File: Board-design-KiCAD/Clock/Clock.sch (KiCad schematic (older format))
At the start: 48 parts, among them M1 SevSeg4Inch, M2 SevSeg4Inch, Y1 SevSeg1.8Inch, Y2 SevSeg1.8Inch, Y3 SevSeg1.8Inch, Y4 SevSeg1.8Inch

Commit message: Update part(s): DS3231 RTC Module
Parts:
- removed RTC1: DS3231-RPi, Custom:DS3231-RPi, symbol Custom:DS3231-RPi
- added RTC1: DS3231-Module, Custom:DS3231-Module, symbol Custom:DS3231-Module
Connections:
- wire segments 281 -> 282
- no-connect marks 51 -> 55
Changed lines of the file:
@@
 Text GLabel 3500 4300 2    50   Input ~ 0
 RTC_SDA
-Text GLabel 1800 8000 2    50   Input ~ 0
+Text GLabel 1800 7900 2    50   Input ~ 0
 RTC_SDA
 Text GLabel 2400 3850 0    50   Input ~ 0
 +3.3V
-Text GLabel 1200 7900 0    50   Input ~ 0
+Text GLabel 1200 7800 0    50   Input ~ 0
 +3.3V
 $Comp
 L power:GND #PWR03
 U 1 1 5F82DF5B
-P 1100 8400
-F 0 "#PWR03" H 1100 8150 50  0001 C CNN
-F 1 "GND" H 1105 8227 50  0000 C CNN
-F 2 "" H 1100 8400 50  0001 C CNN
-F 3 "" H 1100 8400 50  0001 C CNN
-	1    1100 8400
+P 1800 8600
+F 0 "#PWR03" H 1800 8350 50  0001 C CNN
+F 1 "GND" H 1805 8427 50  0000 C CNN
+F 2 "" H 1800 8600 50  0001 C CNN
+F 3 "" H 1800 8600 50  0001 C CNN
+	1    1800 8600
 	1    0    0    -1
 $EndComp
@@
 NoConn ~ 3400 6750
 NoConn ~ 3400 6850
-$Comp
-L Custom:DS3231-RPi RTC1
-U 1 1 5F952233
-P 1500 8100
-F 0 "RTC1" H 1500 8565 50  0000 C CNN
-F 1 "DS3231-RPi" H 1500 8474 50  0000 C CNN
-F 2 "Custom:DS3231-RPi" H 1500 8200 50  0001 C CNN
-F 3 "" H 1500 8200 50  0001 C CNN
-	1    1500 8100
-	1    0    0    -1
-$EndComp
-Wire Wire Line
-	1100 8400 1100 8300
-Wire Wire Line
-	1100 8300 1200 8300
 $Comp
 L Regulator_Linear:LM1117-3.3 Regulator-3.3V1
@@
 	1    0    0    -1
 $EndComp
+$Comp
+L Custom:DS3231-Module RTC1
+U 1 1 5F69BB73
+P 1500 8150
+F 0 "RTC1" H 1500 8765 50  0000 C CNN
+F 1 "DS3231-Module" H 1500 8674 50  0000 C CNN
+F 2 "Custom:DS3231-Module" H 1500 8400 50  0001 C CNN
+F 3 "" H 1500 8400 50  0001 C CNN
+	1    1500 8150
+	1    0    0    -1
+$EndComp
+Wire Wire Line
+	1800 8400 1800 8500
+Wire Wire Line
+	1800 8500 1800 8600
+Connection ~ 1800 8500
+Wire Wire Line
+	1200 7800 1200 7900
+NoConn ~ 1200 8350
+NoConn ~ 1200 8250
+NoConn ~ 1800 7800
+NoConn ~ 1800 8100
 Wire Bus Line
 	10450 2850 10450 3850

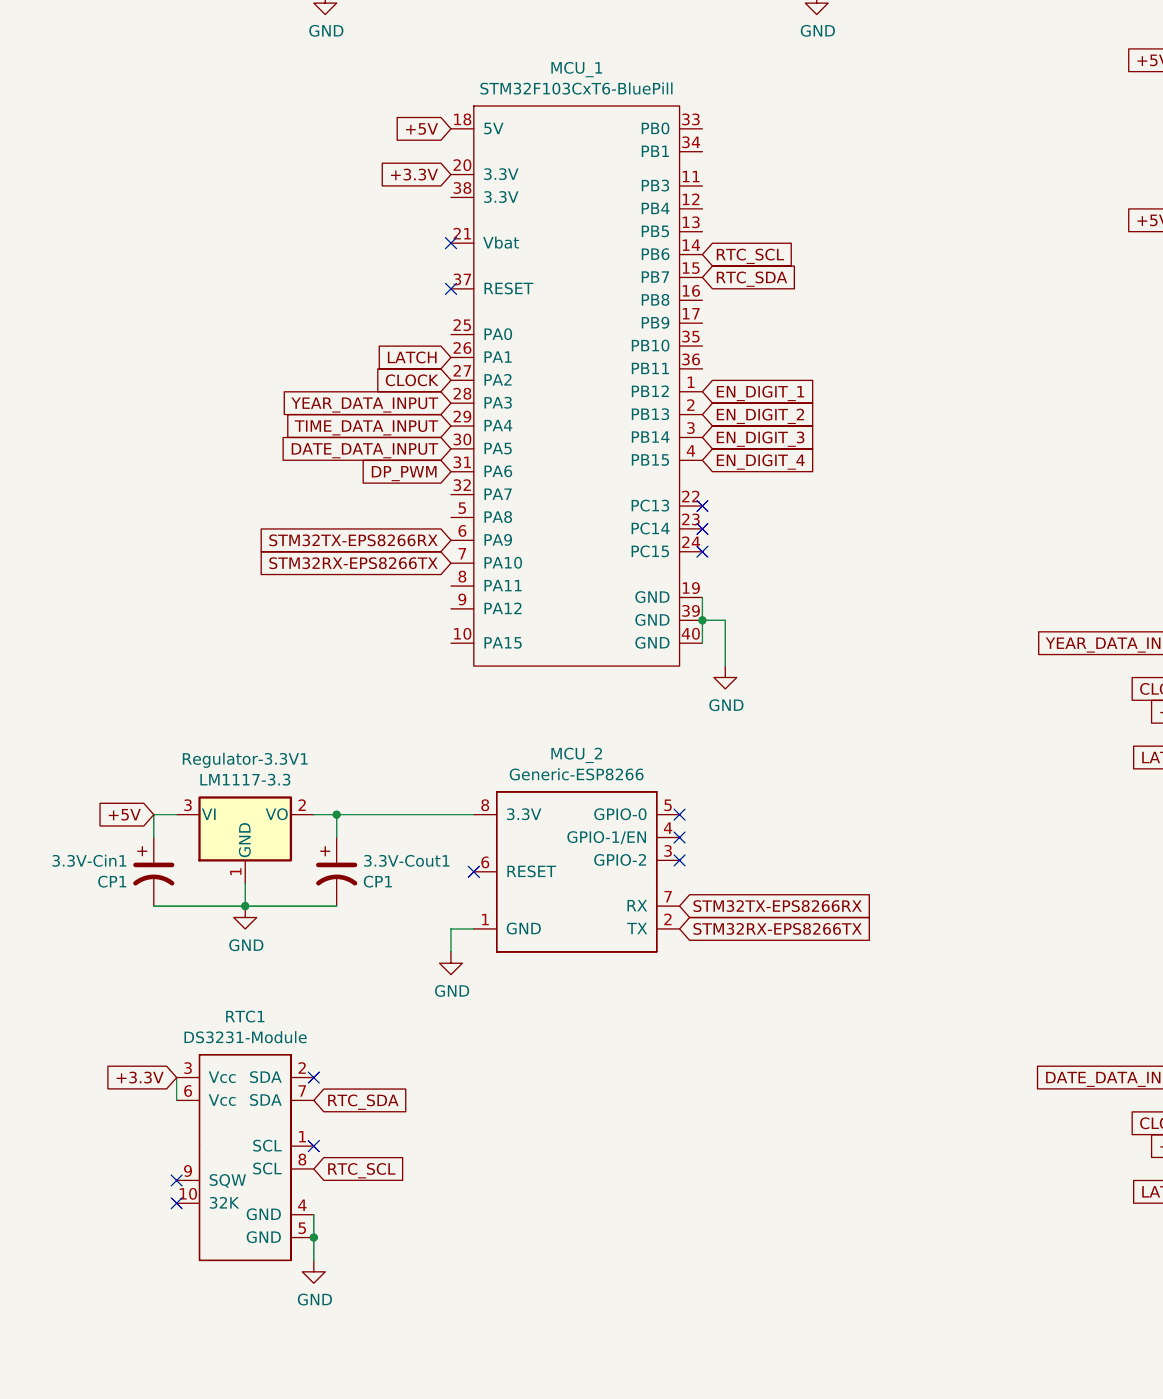
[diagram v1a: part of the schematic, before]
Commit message: Add credential reset button for ESP8266
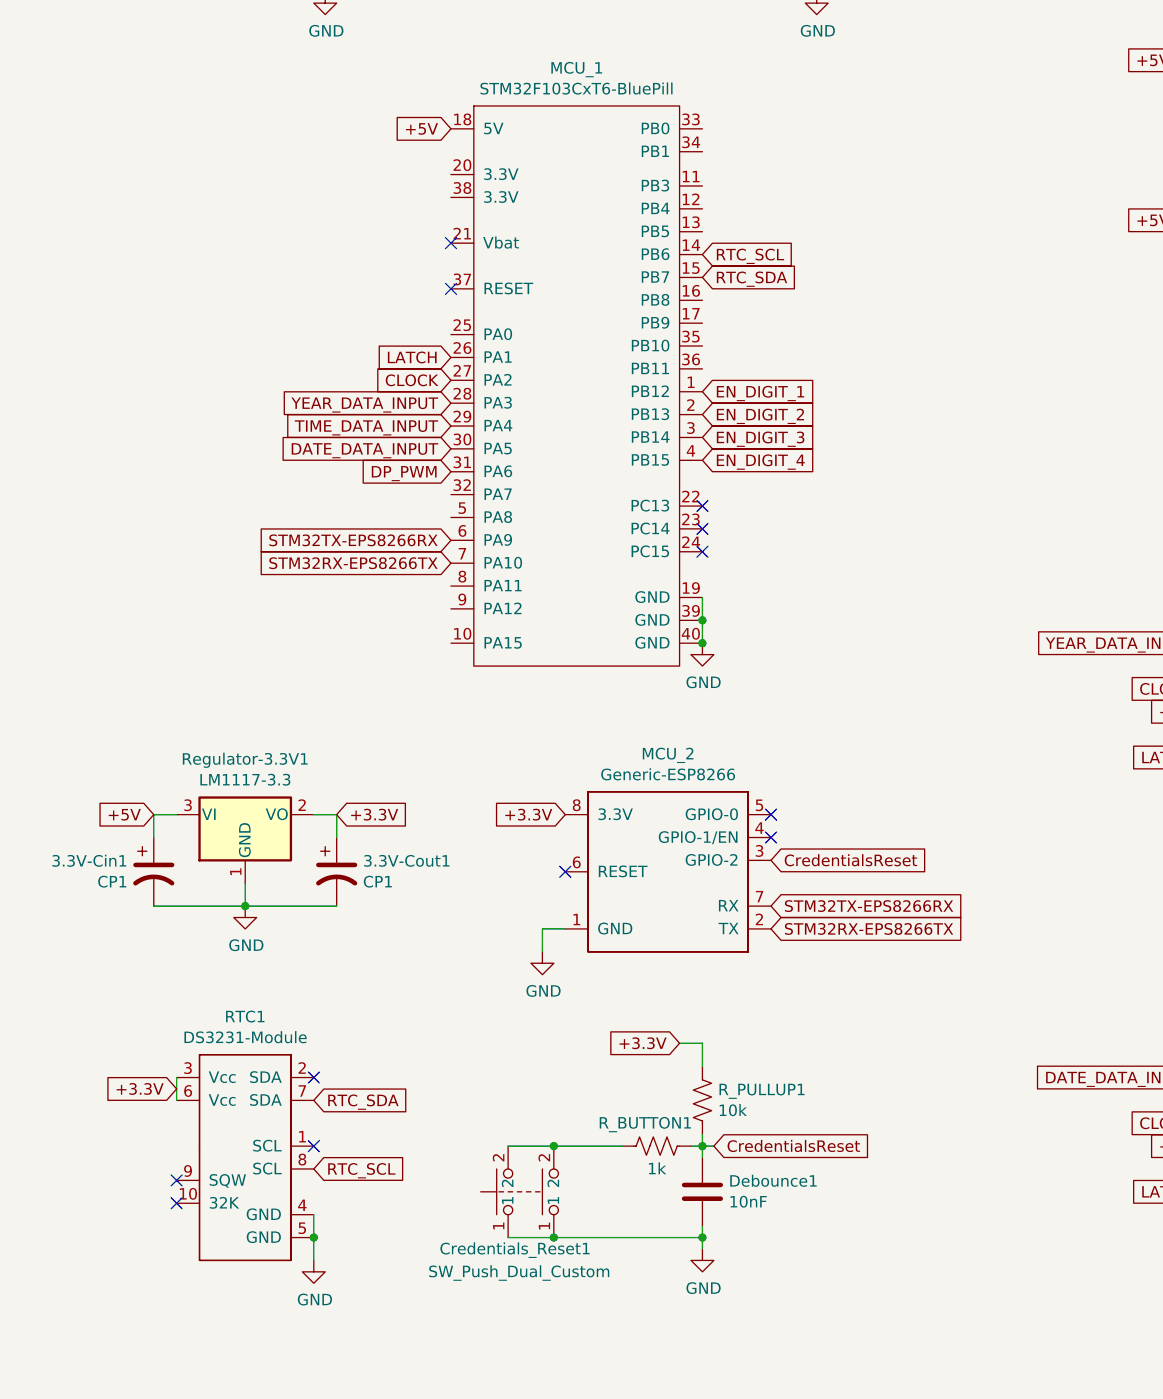
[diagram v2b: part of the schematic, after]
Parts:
- added Credentials_Reset1: SW_Push_Dual_Custom, Button_Switch_THT:SW_PUSH-12mm_Wuerth-430476085716, symbol Custom:SW_Push_Dual_Custom
- added Debounce1: 10nF, Capacitor_THT:C_Disc_D5.0mm_W2.5mm_P5.00mm, symbol Device:C
- added R_BUTTON1: 1k, Resistor_THT:R_Axial_DIN0207_L6.3mm_D2.5mm_P10.16mm_Horizontal, symbol Device:R_US
- added R_PULLUP1: 10k, Resistor_THT:R_Axial_DIN0207_L6.3mm_D2.5mm_P10.16mm_Horizontal, symbol Device:R_US
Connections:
- net +3.3V: now also 3.3V-Cout1.1, MCU_2.8 (3.3V), Regulator-3.3V1.2 (VO), R_PULLUP1.1; no longer MCU_1.20 (3.3V)
- net GND: now also Credentials_Reset1.1, Debounce1.2
- net CredentialsReset: now reaches MCU_2.3 (GPIO-2)
- net CredentialsReset: now also Debounce1.1, R_BUTTON1.2, R_PULLUP1.2
- new net: Credentials_Reset1.2, R_BUTTON1.1
- no-connect marks 55 -> 54
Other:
- moved on the sheet: MCU_2
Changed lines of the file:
@@
 L power:GND #PWR01
 U 1 1 5F6AF068
-P 3600 6000
-F 0 "#PWR01" H 3600 5750 50  0001 C CNN
-F 1 "GND" H 3605 5827 50  0000 C CNN
-F 2 "" H 3600 6000 50  0001 C CNN
-F 3 "" H 3600 6000 50  0001 C CNN
-	1    3600 6000
+P 3500 5900
+F 0 "#PWR01" H 3500 5650 50  0001 C CNN
+F 1 "GND" H 3505 5727 50  0000 C CNN
+F 2 "" H 3500 5900 50  0001 C CNN
+F 3 "" H 3500 5900 50  0001 C CNN
+	1    3500 5900
 	1    0    0    -1
 $EndComp
@@
 	3500 5800 3500 5900
 Connection ~ 3500 5800
-Wire Wire Line
-	3600 6000 3600 5800
-Wire Wire Line
-	3600 5800 3500 5800
 Text GLabel 2400 5150 0    50   Input ~ 0
 DP_PWM
@@
 L Custom:Generic-ESP8266 MCU_2
 U 1 1 5F825E1F
-P 2950 6750
-F 0 "MCU_2" H 2950 7115 50  0000 C CNN
-F 1 "Generic-ESP8266" H 2950 7024 50  0000 C CNN
-F 2 "Custom:Generic-ESP8266" H 2700 6750 50  0001 C CNN
-F 3 "" H 2700 6750 50  0001 C CNN
-	1    2950 6750
+P 3350 6750
+F 0 "MCU_2" H 3350 7115 50  0000 C CNN
+F 1 "Generic-ESP8266" H 3350 7024 50  0000 C CNN
+F 2 "Custom:Generic-ESP8266" H 3100 6750 50  0001 C CNN
+F 3 "" H 3100 6750 50  0001 C CNN
+	1    3350 6750
 	1    0    0    -1
 $EndComp
@@
 Text GLabel 1800 7900 2    50   Input ~ 0
 RTC_SDA
-Text GLabel 2400 3850 0    50   Input ~ 0
+Text GLabel 1900 6650 2    50   Input ~ 0
 +3.3V
-Text GLabel 1200 7800 0    50   Input ~ 0
+Text GLabel 1200 7850 0    50   Input ~ 0
 +3.3V
 $Comp
@@
 Text GLabel 2400 5550 0    50   Input ~ 0
 STM32RX-EPS8266TX
-Text GLabel 3400 7050 2    50   Input ~ 0
+Text GLabel 3800 7050 2    50   Input ~ 0
 STM32TX-EPS8266RX
-Text GLabel 3400 7150 2    50   Input ~ 0
+Text GLabel 3800 7150 2    50   Input ~ 0
 STM32RX-EPS8266TX
 $Comp
 L power:GND #PWR02
 U 1 1 5F84B160
-P 2400 7250
-F 0 "#PWR02" H 2400 7000 50  0001 C CNN
-F 1 "GND" H 2405 7077 50  0000 C CNN
-F 2 "" H 2400 7250 50  0001 C CNN
-F 3 "" H 2400 7250 50  0001 C CNN
-	1    2400 7250
-	1    0    0    -1
-$EndComp
-Wire Wire Line
-	2400 7250 2400 7150
-Wire Wire Line
-	2400 7150 2500 7150
-NoConn ~ 2500 6900
-NoConn ~ 3400 6650
-NoConn ~ 3400 6750
-NoConn ~ 3400 6850
+P 2800 7250
+F 0 "#PWR02" H 2800 7000 50  0001 C CNN
+F 1 "GND" H 2805 7077 50  0000 C CNN
+F 2 "" H 2800 7250 50  0001 C CNN
+F 3 "" H 2800 7250 50  0001 C CNN
+	1    2800 7250
+	1    0    0    -1
+$EndComp
+Wire Wire Line
+	2800 7250 2800 7150
+Wire Wire Line
+	2800 7150 2900 7150
+NoConn ~ 2900 6900
+NoConn ~ 3800 6650
+NoConn ~ 3800 6750
 $Comp
 L Regulator_Linear:LM1117-3.3 Regulator-3.3V1
@@
 Text GLabel 1100 6650 0    50   Input ~ 0
 +5V
-Wire Wire Line
-	1900 6650 2500 6650
-Connection ~ 1900 6650
 $Comp
 L power:GND #PWR04
@@
 NoConn ~ 1800 7800
 NoConn ~ 1800 8100
+Text GLabel 2900 6650 0    50   Input ~ 0
++3.3V
+$Comp
+L Device:C Debounce1
+U 1 1 5F763DEB
+P 3500 8300
+F 0 "Debounce1" H 3615 8346 50  0000 L CNN
+F 1 "10nF" H 3615 8255 50  0000 L CNN
+F 2 "Capacitor_THT:C_Disc_D5.0mm_W2.5mm_P5.00mm" H 3538 8150 50  0001 C CNN
+F 3 "~" H 3500 8300 50  0001 C CNN
+	1    3500 8300
+	1    0    0    -1
+$EndComp
+$Comp
+L power:GND #PWR0119
+U 1 1 5F765C62
+P 3500 8550
+F 0 "#PWR0119" H 3500 8300 50  0001 C CNN
+F 1 "GND" H 3505 8377 50  0000 C CNN
+F 2 "" H 3500 8550 50  0001 C CNN
+F 3 "" H 3500 8550 50  0001 C CNN
+	1    3500 8550
+	1    0    0    -1
+$EndComp
+$Comp
+L Device:R_US R_PULLUP1
+U 1 1 5F766377
+P 3500 7900
+F 0 "R_PULLUP1" H 3568 7946 50  0000 L CNN
+F 1 "10k" H 3568 7855 50  0000 L CNN
+F 2 "Resistor_THT:R_Axial_DIN0207_L6.3mm_D2.5mm_P10.16mm_Horizontal" V 3540 7890 50  0001 C CNN
+F 3 "~" H 3500 7900 50  0001 C CNN
+	1    3500 7900
+	1    0    0    -1
+$EndComp
+$Comp
+L Device:R_US R_BUTTON1
+U 1 1 5F767A96
+P 3300 8100
+F 0 "R_BUTTON1" V 3400 8150 50  0000 C CNN
+F 1 "1k" V 3200 8100 50  0000 C CNN
+F 2 "Resistor_THT:R_Axial_DIN0207_L6.3mm_D2.5mm_P10.16mm_Horizontal" V 3340 8090 50  0001 C CNN
+F 3 "~" H 3300 8100 50  0001 C CNN
+	1    3300 8100
+	0    -1   -1   0
+$EndComp
+Text GLabel 3400 7650 0    50   Input ~ 0
++3.3V
+Wire Wire Line
+	3500 8050 3500 8100
+Wire Wire Line
+	3500 8100 3450 8100
+Wire Wire Line
+	3500 8150 3500 8100
+Connection ~ 3500 8100
+Wire Wire Line
+	3400 7650 3500 7650
+Wire Wire Line
+	3500 7650 3500 7750
+Connection ~ 3500 5900
+Wire Wire Line
+	3500 8500 3500 8550
+Wire Wire Line
+	3500 8500 3500 8450
+Connection ~ 3500 8500
+Text GLabel 3550 8100 2    50   Input ~ 0
+CredentialsReset
+Text GLabel 3800 6850 2    50   Input ~ 0
+CredentialsReset
+Wire Wire Line
+	3550 8100 3500 8100
+Wire Wire Line
+	2850 8500 3500 8500
+Wire Wire Line
+	2850 8100 3150 8100
+$Comp
+L Custom:SW_Push_Dual_Custom Credentials_Reset1
+U 1 1 5F9F281E
+P 2700 8300
+F 0 "Credentials_Reset1" V 2450 8650 50  0000 R CNN
+F 1 "SW_Push_Dual_Custom" V 2350 8700 50  0000 R CNN
+F 2 "Button_Switch_THT:SW_PUSH-12mm_Wuerth-430476085716" H 2700 8300 50  0001 C CNN
+F 3 "" H 2700 8300 50  0001 C CNN
+	1    2700 8300
+	0    -1   -1   0
+$EndComp
+Wire Wire Line
+	2650 8500 2850 8500
+Connection ~ 2850 8500
+Wire Wire Line
+	2650 8100 2850 8100
 Wire Bus Line
 	10450 2850 10450 3850
@@
 Wire Bus Line
 	8800 7400 8800 8500
+Connection ~ 2850 8100
 $EndSCHEMATC

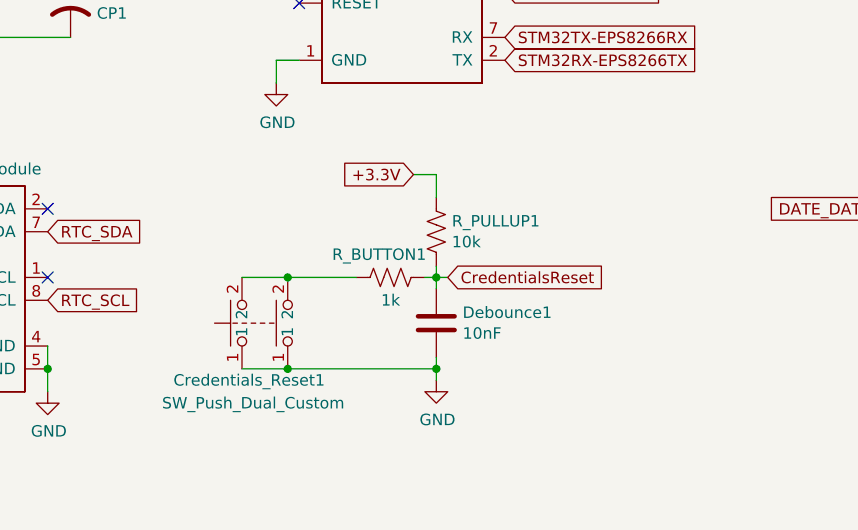
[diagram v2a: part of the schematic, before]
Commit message: Modify button circuit and build code for button management.
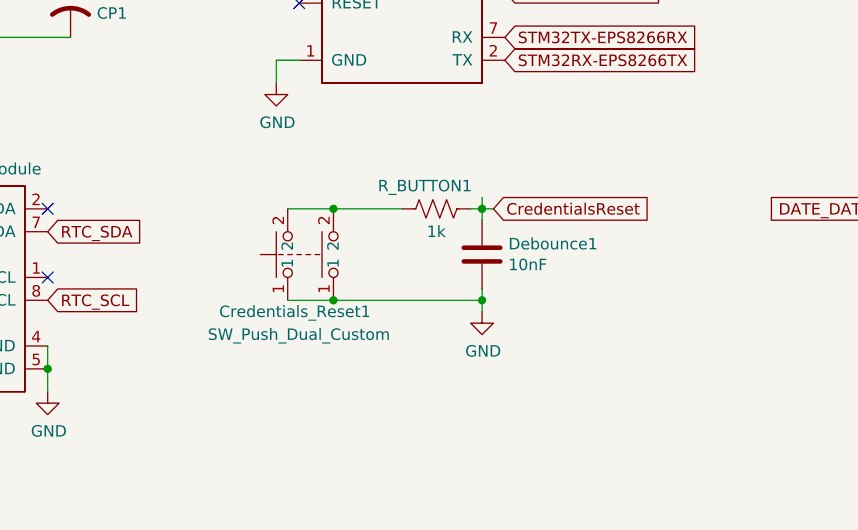
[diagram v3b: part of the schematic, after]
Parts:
- removed R_PULLUP1: 10k, Resistor_THT:R_Axial_DIN0207_L6.3mm_D2.5mm_P10.16mm_Horizontal, symbol Device:R_US
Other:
- moved on the sheet: Credentials_Reset1, Debounce1, R_BUTTON1
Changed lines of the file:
@@
 	2800 7150 2900 7150
 NoConn ~ 2900 6900
-NoConn ~ 3800 6650
 NoConn ~ 3800 6750
 $Comp
@@
 L Device:C Debounce1
 U 1 1 5F763DEB
-P 3500 8300
-F 0 "Debounce1" H 3615 8346 50  0000 L CNN
-F 1 "10nF" H 3615 8255 50  0000 L CNN
-F 2 "Capacitor_THT:C_Disc_D5.0mm_W2.5mm_P5.00mm" H 3538 8150 50  0001 C CNN
-F 3 "~" H 3500 8300 50  0001 C CNN
-	1    3500 8300
+P 3700 8000
+F 0 "Debounce1" H 3815 8046 50  0000 L CNN
+F 1 "10nF" H 3815 7955 50  0000 L CNN
+F 2 "Capacitor_THT:C_Disc_D5.0mm_W2.5mm_P5.00mm" H 3738 7850 50  0001 C CNN
+F 3 "~" H 3700 8000 50  0001 C CNN
+	1    3700 8000
 	1    0    0    -1
 $EndComp
@@
 L power:GND #PWR0119
 U 1 1 5F765C62
-P 3500 8550
-F 0 "#PWR0119" H 3500 8300 50  0001 C CNN
-F 1 "GND" H 3505 8377 50  0000 C CNN
-F 2 "" H 3500 8550 50  0001 C CNN
-F 3 "" H 3500 8550 50  0001 C CNN
-	1    3500 8550
-	1    0    0    -1
-$EndComp
-$Comp
-L Device:R_US R_PULLUP1
-U 1 1 5F766377
-P 3500 7900
-F 0 "R_PULLUP1" H 3568 7946 50  0000 L CNN
-F 1 "10k" H 3568 7855 50  0000 L CNN
-F 2 "Resistor_THT:R_Axial_DIN0207_L6.3mm_D2.5mm_P10.16mm_Horizontal" V 3540 7890 50  0001 C CNN
-F 3 "~" H 3500 7900 50  0001 C CNN
-	1    3500 7900
+P 3700 8250
+F 0 "#PWR0119" H 3700 8000 50  0001 C CNN
+F 1 "GND" H 3705 8077 50  0000 C CNN
+F 2 "" H 3700 8250 50  0001 C CNN
+F 3 "" H 3700 8250 50  0001 C CNN
+	1    3700 8250
 	1    0    0    -1
 $EndComp
@@
 L Device:R_US R_BUTTON1
 U 1 1 5F767A96
-P 3300 8100
-F 0 "R_BUTTON1" V 3400 8150 50  0000 C CNN
-F 1 "1k" V 3200 8100 50  0000 C CNN
-F 2 "Resistor_THT:R_Axial_DIN0207_L6.3mm_D2.5mm_P10.16mm_Horizontal" V 3340 8090 50  0001 C CNN
-F 3 "~" H 3300 8100 50  0001 C CNN
-	1    3300 8100
+P 3500 7800
+F 0 "R_BUTTON1" V 3600 7850 50  0000 C CNN
+F 1 "1k" V 3400 7800 50  0000 C CNN
+F 2 "Resistor_THT:R_Axial_DIN0207_L6.3mm_D2.5mm_P10.16mm_Horizontal" V 3540 7790 50  0001 C CNN
+F 3 "~" H 3500 7800 50  0001 C CNN
+	1    3500 7800
 	0    -1   -1   0
 $EndComp
-Text GLabel 3400 7650 0    50   Input ~ 0
-+3.3V
-Wire Wire Line
-	3500 8050 3500 8100
-Wire Wire Line
-	3500 8100 3450 8100
-Wire Wire Line
-	3500 8150 3500 8100
-Connection ~ 3500 8100
-Wire Wire Line
-	3400 7650 3500 7650
-Wire Wire Line
-	3500 7650 3500 7750
+Wire Wire Line
+	3700 7750 3700 7800
+Wire Wire Line
+	3700 7800 3650 7800
+Wire Wire Line
+	3700 7850 3700 7800
+Connection ~ 3700 7800
 Connection ~ 3500 5900
 Wire Wire Line
-	3500 8500 3500 8550
-Wire Wire Line
-	3500 8500 3500 8450
-Connection ~ 3500 8500
-Text GLabel 3550 8100 2    50   Input ~ 0
+	3700 8200 3700 8250
+Wire Wire Line
+	3700 8200 3700 8150
+Connection ~ 3700 8200
+Text GLabel 3750 7800 2    50   Input ~ 0
 CredentialsReset
+Wire Wire Line
+	3750 7800 3700 7800
+Wire Wire Line
+	3050 8200 3700 8200
+Wire Wire Line
+	3050 7800 3350 7800
+$Comp
+L Custom:SW_Push_Dual_Custom Credentials_Reset1
+U 1 1 5F9F281E
+P 2900 8000
+F 0 "Credentials_Reset1" V 2650 8350 50  0000 R CNN
+F 1 "SW_Push_Dual_Custom" V 2550 8400 50  0000 R CNN
+F 2 "Button_Switch_THT:SW_PUSH-12mm_Wuerth-430476085716" H 2900 8000 50  0001 C CNN
+F 3 "" H 2900 8000 50  0001 C CNN
+	1    2900 8000
+	0    -1   -1   0
+$EndComp
+Wire Wire Line
+	2850 8200 3050 8200
+Connection ~ 3050 8200
+Wire Wire Line
+	2850 7800 3050 7800
+Connection ~ 3050 7800
 Text GLabel 3800 6850 2    50   Input ~ 0
 CredentialsReset
-Wire Wire Line
-	3550 8100 3500 8100
-Wire Wire Line
-	2850 8500 3500 8500
-Wire Wire Line
-	2850 8100 3150 8100
-$Comp
-L Custom:SW_Push_Dual_Custom Credentials_Reset1
-U 1 1 5F9F281E
-P 2700 8300
-F 0 "Credentials_Reset1" V 2450 8650 50  0000 R CNN
-F 1 "SW_Push_Dual_Custom" V 2350 8700 50  0000 R CNN
-F 2 "Button_Switch_THT:SW_PUSH-12mm_Wuerth-430476085716" H 2700 8300 50  0001 C CNN
-F 3 "" H 2700 8300 50  0001 C CNN
-	1    2700 8300
-	0    -1   -1   0
-$EndComp
-Wire Wire Line
-	2650 8500 2850 8500
-Connection ~ 2850 8500
-Wire Wire Line
-	2650 8100 2850 8100
+NoConn ~ 3800 6650
+Wire Bus Line
+	10000 8750 13950 8750
+Wire Bus Line
+	13950 7900 13950 8750
+Wire Bus Line
+	10000 6850 13950 6850
+Wire Bus Line
+	13950 6000 13950 6850
 Wire Bus Line
 	10450 2850 10450 3850
 Wire Bus Line
-	13950 6000 13950 6850
-Wire Bus Line
-	10000 6850 13950 6850
-Wire Bus Line
-	13950 7900 13950 8750
-Wire Bus Line
-	10000 8750 13950 8750
-Wire Bus Line
 	12000 1200 12000 2050
 Wire Bus Line
@@
 	10050 7400 10050 8250
 Wire Bus Line
+	8800 7400 8800 8500
+Wire Bus Line
 	8800 5500 8800 6600
 Wire Bus Line
 	10750 1200 10750 2400
-Wire Bus Line
-	8800 7400 8800 8500
-Connection ~ 2850 8100
 $EndSCHEMATC
